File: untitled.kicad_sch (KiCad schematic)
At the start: 6 parts, among them J13 HDMI_A_1.4, J3 Bus_M.2_Socket_M, J5 USB3_A, J6 USB3_A, M1 M.2 Screw

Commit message: At home update
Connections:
- net GND: now also J5.10 (SHIELD), J5.A4 (GND), J5.A7 (DRAIN), J5.B4 (GND), J5.B7 (DRAIN), J6.10 (SHIELD), J6.A4 (GND), J6.A7 (DRAIN), J6.B4 (GND), J6.B7 (DRAIN), Module1.192 (GND)
- net at Module1.110 (PCIe_CLK_P): now also J3.55 (REFCLKp)
- net at Module1.112 (PCIe_CLK_N): now also J3.53 (REFCLKn)
- net +3.3v renamed +3.3V
- net +5v renamed +5V
- no-connect marks 105 -> 101

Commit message: Work Changes and documentation
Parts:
- removed J6: USB3_A, StackedUSBPretty:MOLEX_484060003, symbol Pi5Compute:USB3_A
- J5: footprint StackedUSBPretty:MOLEX_484060003 -> CM5IO:MTCONN_UBAF30-D2011
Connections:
- net Sim7600_DN renamed USB_DN
- net Sim7600_DP renamed USB_DP
- no-connect marks 101 -> 97

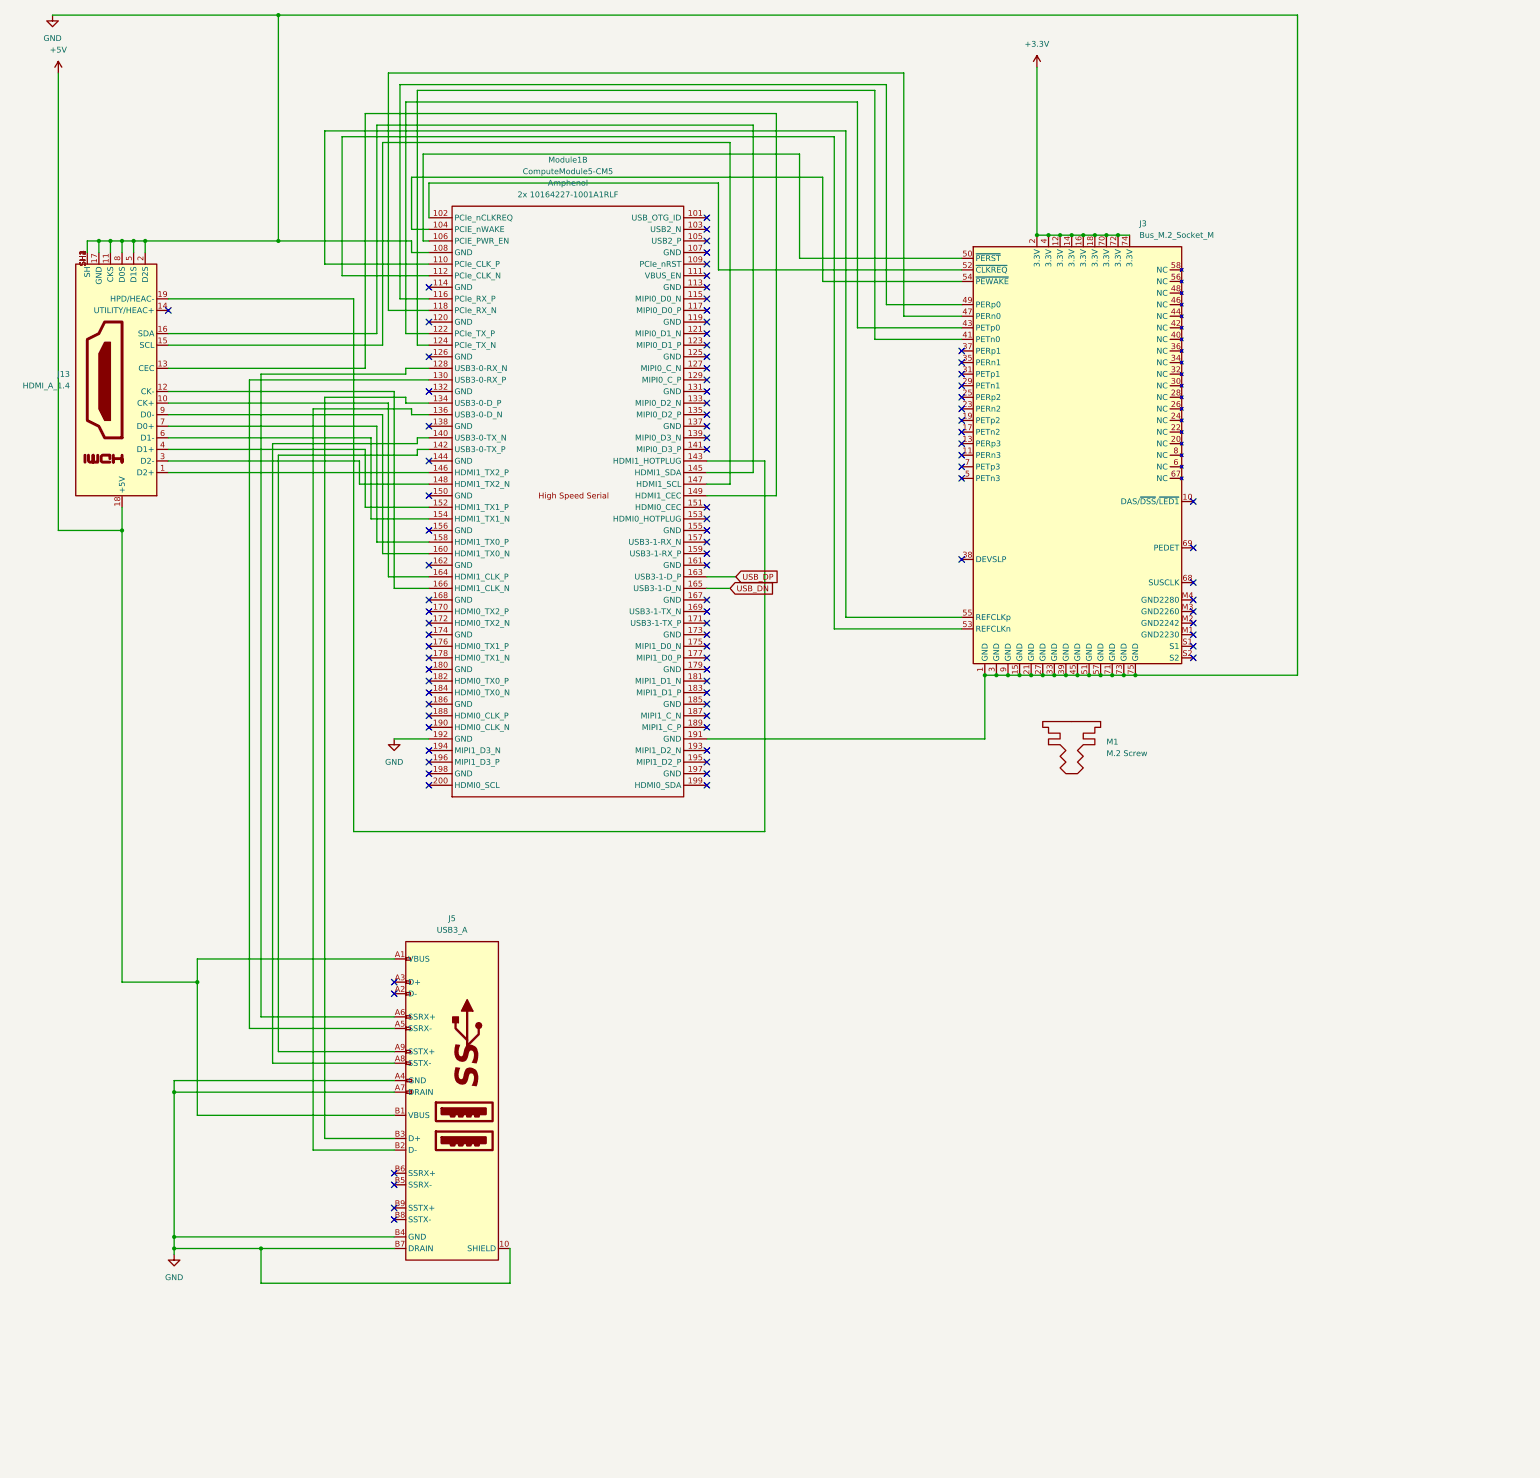
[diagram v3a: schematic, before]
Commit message: Updated to CM5 Doc
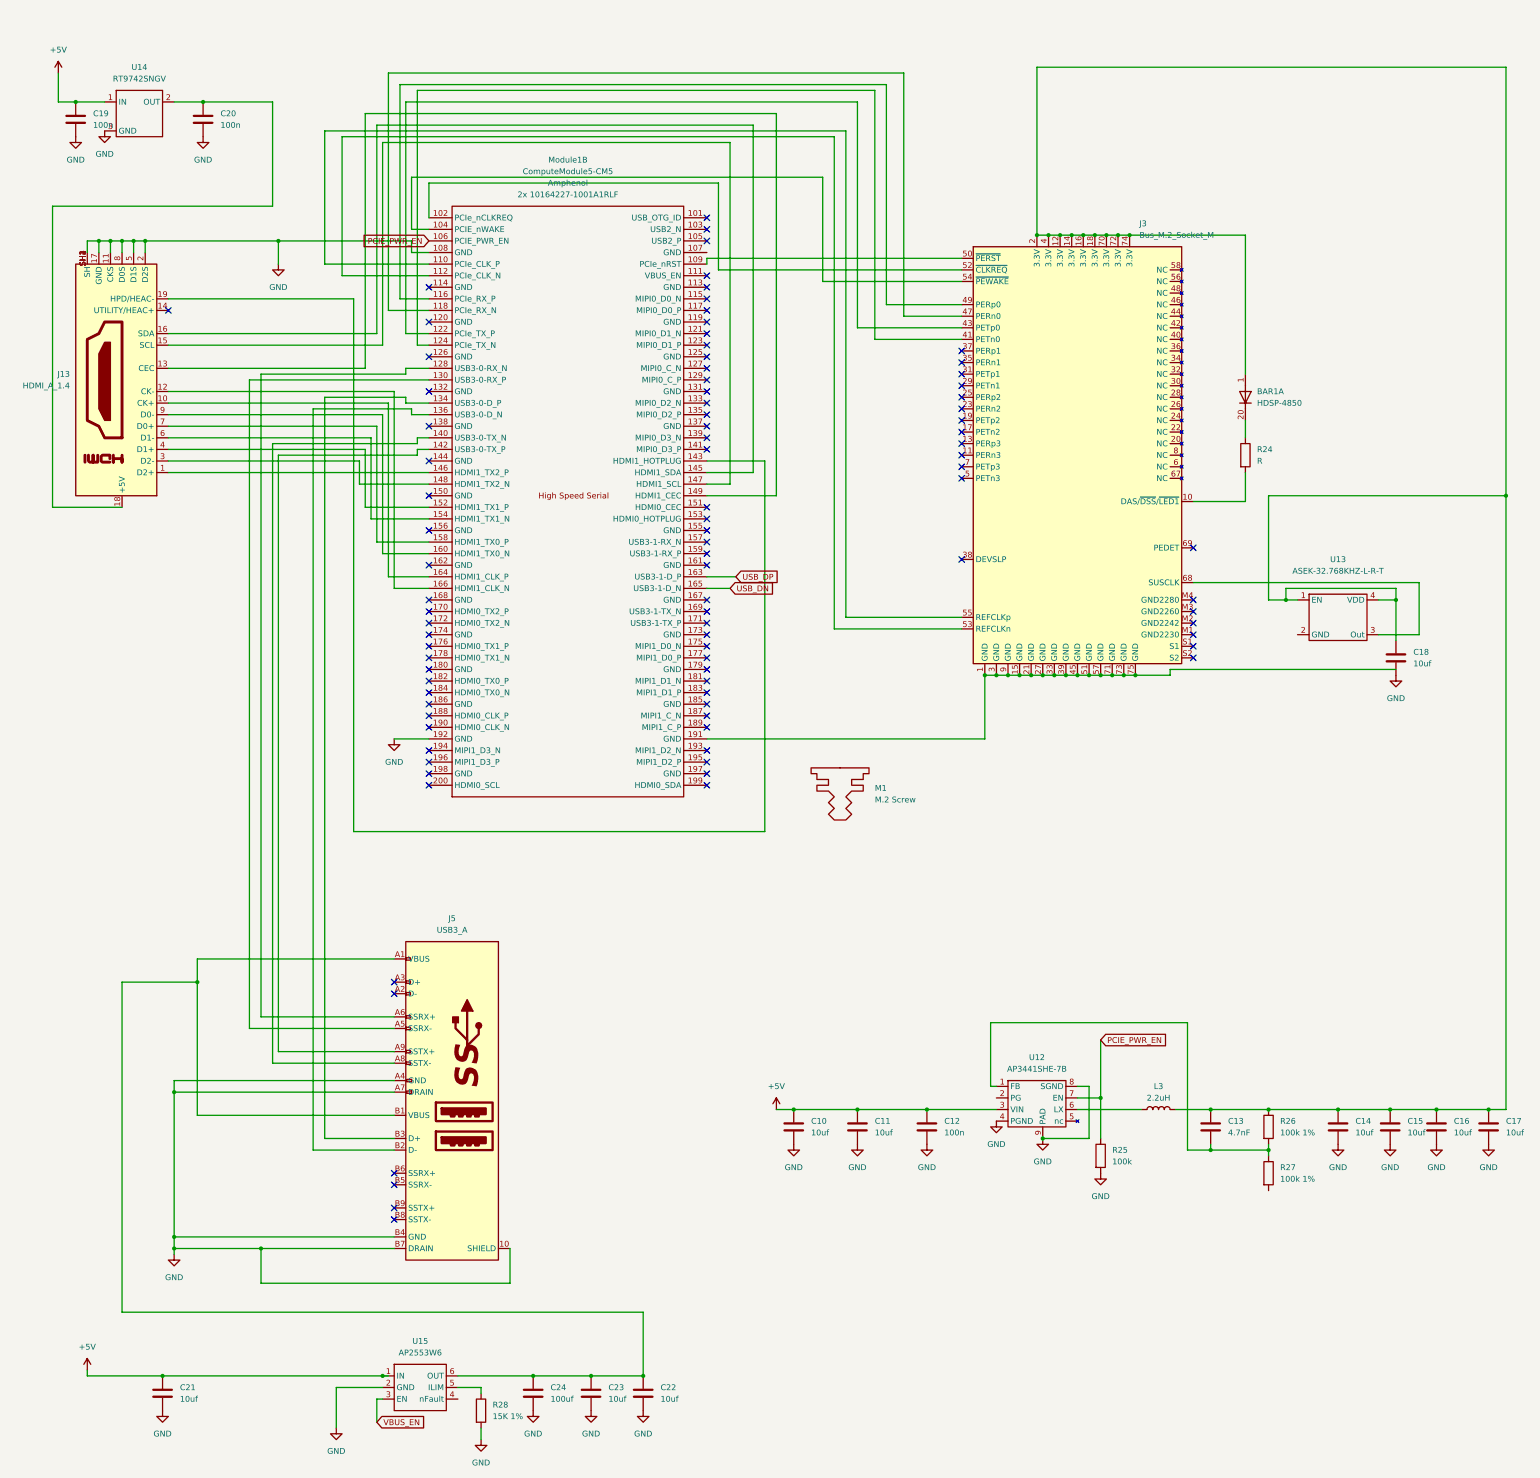
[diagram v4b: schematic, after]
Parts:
- added BAR1: HDSP-4850, Display:HDSP-4850, symbol LED:HDSP-4850
- added C10, C11, C14, C15, C16, C17, C18, C21, C22, C23: 10uf, symbol Device:C
- added C12, C19, C20: 100n, symbol Device:C
- added C13: 4.7nF, symbol Device:C
- added C24: 100uf, symbol Device:C
- added L3: 2.2uH, symbol Device:L
- added R24: R, symbol Device:R
- added R25: 100k, symbol Device:R
- added R26, R27: 100k 1%, symbol Device:R
- added R28: 15K 1%, symbol Device:R
- added U12: AP3441SHE-7B, Package_DFN_QFN:DFN-8-1EP_2x2mm_P0.5mm_EP1.05x1.75mm, symbol Pi5Compute:AP3441SHE-7B
- added U13: ASEK-32.768KHZ-L-R-T, Crystal:Crystal_SMD_3225-4Pin_3.2x2.5mm, symbol Pi5Compute:ASEK-32.768KHZ-L-R-T
- added U14: RT9742SNGV, Package_TO_SOT_SMD:TSOT-23_HandSoldering, symbol Pi5Compute:RT9742SNGV
- added U15: AP2553W6, Package_TO_SOT_SMD:SOT-23-6, symbol Pi5Compute:AP2553W6
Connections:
- net +5V: now also C10.1, C11.1, C12.1, C19.1, C21.1, U12.3 (VIN), U14.1 (IN), U15.1 (IN); no longer J13.18 (+5V), J5.A1 (VBUS), J5.B1 (VBUS)
- net GND: now also C10.2, C11.2, C12.2, C14.2, C15.2, C16.2, C17.2, C18.2, C19.2, C20.2, C21.2, C22.2, C23.2, C24.2, R25.2, R28.2, U12.4 (PGND), U12.8 (SGND), U12.9 (PAD), U14.3 (GND), U15.2 (GND); no longer J3.1 (GND), J3.15 (GND), J3.21 (GND), J3.27 (GND), J3.3 (GND), J3.33 (GND), J3.39 (GND), J3.45 (GND), J3.51 (GND), J3.57 (GND), J3.71 (GND), J3.73 (GND), J3.75 (GND), J3.9 (GND), Module1.191 (GND)
- net at J3.50 (~{PERST}): now also Module1.109 (PCIe_nRST); no longer Module1.106 (PCIE_PWR_EN)
- net at J3.10 (DAS/~{DSS}/~{LED1}): now also R24.2
- net at J3.68 (SUSCLK): now also U13.3 (Out)
- net +3.3V: no longer names the net of J3.12 (3.3V), J3.14 (3.3V), J3.16 (3.3V), J3.18 (3.3V), J3.2 (3.3V), J3.4 (3.3V), J3.70 (3.3V), J3.72 (3.3V), J3.74 (3.3V)
- net +3.3V: now also BAR1.1 (A), C13.1, C14.1, C15.1, C16.1, C17.1, C18.1, L3.2, R26.1, U13.1 (EN), U13.4 (VDD)
- new net: C22.1, C23.1, C24.1, J5.A1 (VBUS), J5.B1 (VBUS), U15.6 (OUT)
- new net: BAR1.20 (K), R24.1
- new net: R28.1, U15.5 (ILIM)
- new net: C20.1, J13.18 (+5V), U14.2 (OUT)
- new net: J3.1 (GND), J3.15 (GND), J3.21 (GND), J3.27 (GND), J3.3 (GND), J3.33 (GND), J3.39 (GND), J3.45 (GND), J3.51 (GND), J3.57 (GND), J3.71 (GND), J3.73 (GND), J3.75 (GND), J3.9 (GND), Module1.191 (GND)
- new net: C13.2, R26.2, R27.1, U12.1 (FB)
- new net: L3.1, U12.6 (LX)
- new net PCIE_PWR_EN: Module1.106 (PCIE_PWR_EN), R25.1, U12.7 (EN)
- new net VBUS_EN: U15.3 (EN)
- no-connect marks 97 -> 93
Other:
- moved on the sheet: M1

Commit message: fixed stuff at home
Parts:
- removed BAR1: HDSP-4850, Display:HDSP-4850, symbol LED:HDSP-4850
- added D1: LED, LED_SMD:LED_0805_2012Metric, symbol Device:LED
- C10, C11, C12, C13, C14, C15, C16, C17, C18, C19, C20, C21, C22, C23, C24: footprint (none) -> Capacitor_SMD:C_0805_2012Metric
- L3: footprint (none) -> Inductor_SMD:L_0805_2012Metric
- R24, R25, R26, R27, R28: footprint (none) -> Resistor_SMD:R_0805_2012Metric
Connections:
- net GND: now also R27.2
- net at C13.1, C14.1, C15.1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: now also D1.2 (A)
- net at R24.1: now also D1.1 (K)
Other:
- moved on the sheet: M1

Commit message: PCIE Changes
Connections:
- net GND: now also J3.1 (GND), J3.15 (GND), J3.21 (GND), J3.27 (GND), J3.3 (GND), J3.33 (GND), J3.39 (GND), J3.45 (GND), J3.51 (GND), J3.57 (GND), J3.71 (GND), J3.73 (GND), J3.75 (GND), J3.9 (GND), Module1.107 (GND), Module1.113 (GND), Module1.114 (GND), Module1.119 (GND), Module1.120 (GND), Module1.125 (GND), Module1.126 (GND), Module1.131 (GND), Module1.132 (GND), Module1.137 (GND), Module1.138 (GND), Module1.144 (GND), Module1.150 (GND), Module1.155 (GND), Module1.156 (GND), Module1.161 (GND), Module1.162 (GND), Module1.167 (GND), Module1.168 (GND), Module1.173 (GND), Module1.174 (GND), Module1.179 (GND), Module1.180 (GND), Module1.185 (GND), Module1.186 (GND), Module1.191 (GND), Module1.197 (GND), Module1.198 (GND), U13.2 (GND)
- net VBUS_EN: now also Module1.111 (VBUS_EN)
- net PER0_P: now reaches J3.49 (PER0_P)
- net PER0_P: now also Module1.124 (PCIe_TX_N); no longer Module1.116 (PCIe_RX_P)
- net PER0_N: now reaches J3.47 (PER0_N)
- net PER0_N: now also Module1.122 (PCIe_TX_P); no longer Module1.118 (PCIe_RX_N)
- net PET0_P: now reaches J3.43 (PET0_P)
- net PET0_P: now also Module1.118 (PCIe_RX_N); no longer Module1.122 (PCIe_TX_P)
- net PET0_N: now reaches J3.41 (PET0_N)
- net PET0_N: now also Module1.116 (PCIe_RX_P); no longer Module1.124 (PCIe_TX_N)
- no-connect marks 93 -> 68

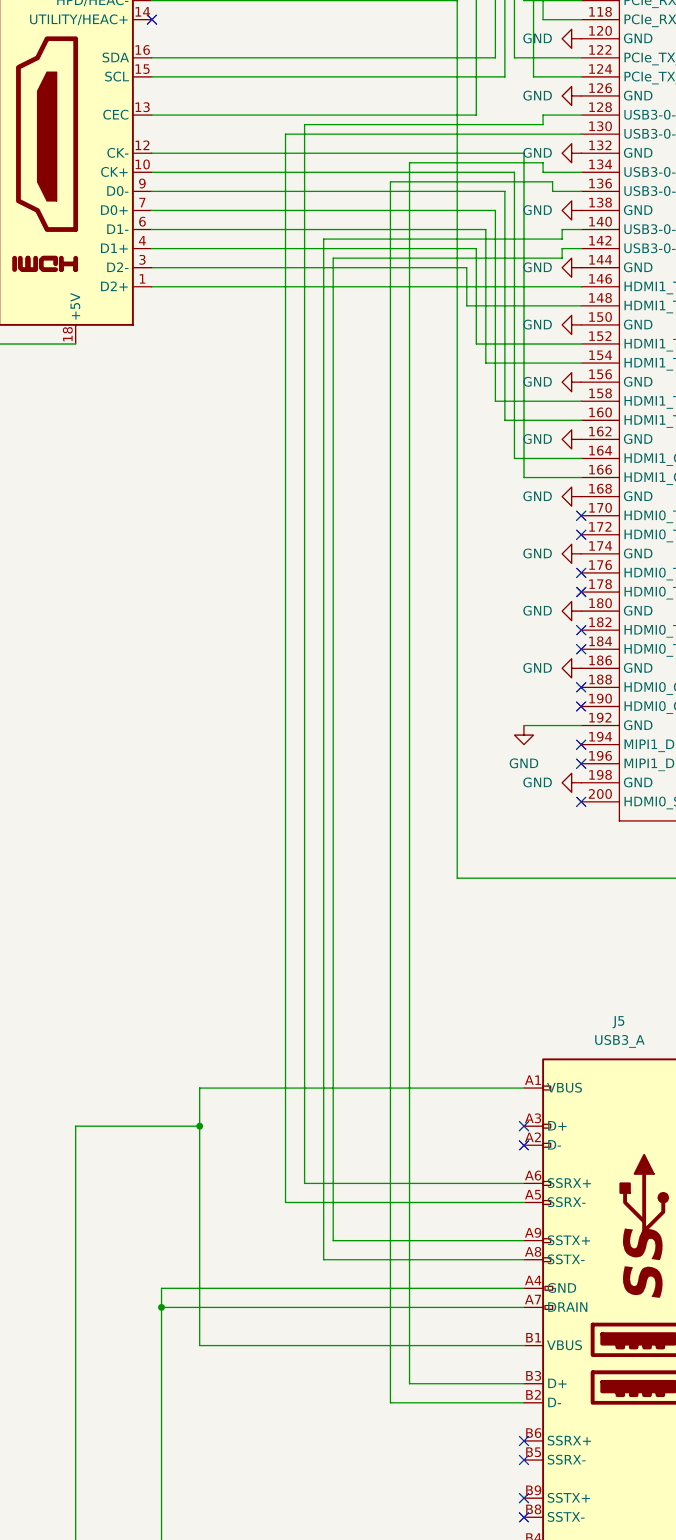
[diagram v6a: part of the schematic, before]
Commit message: Fixes from datasheets
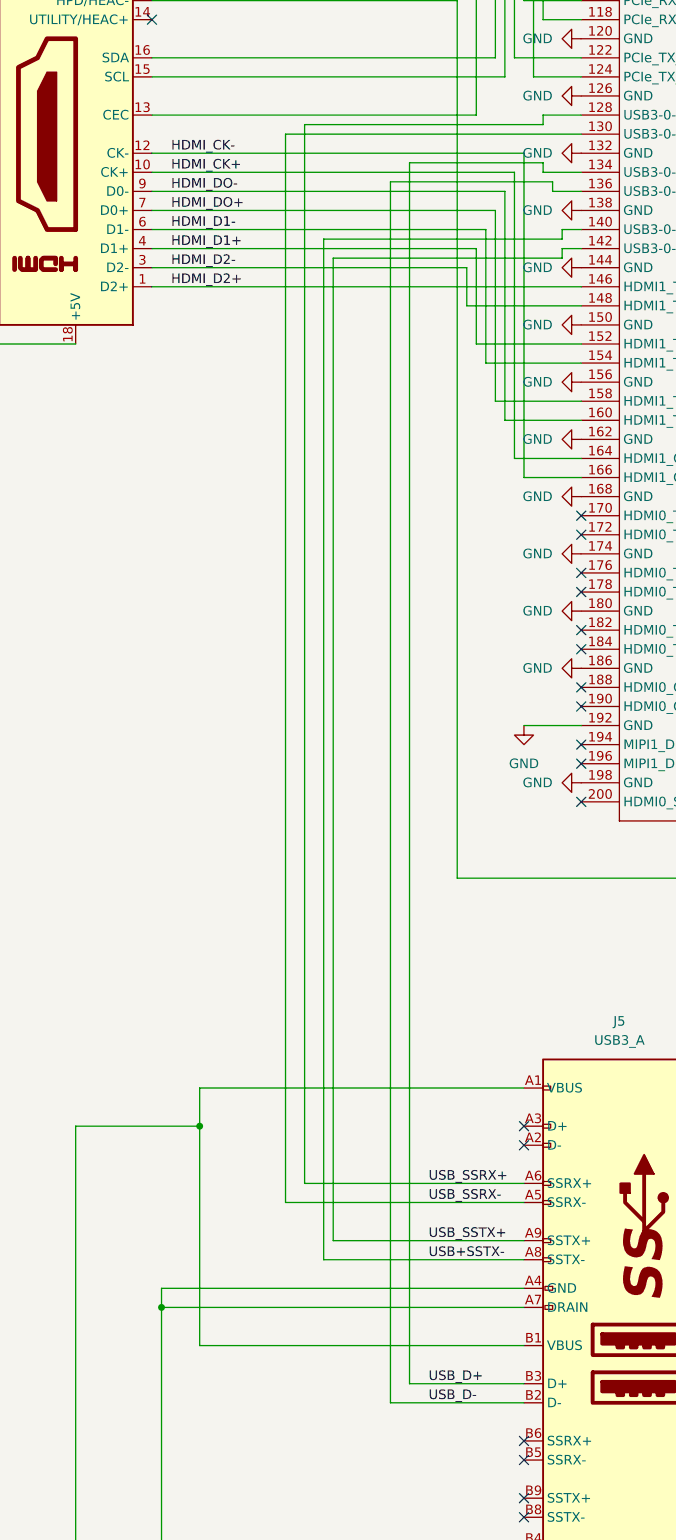
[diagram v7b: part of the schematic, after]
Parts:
- J13: footprint Connector_Video:HDMI_A_Amphenol_10029449-x01xLF_Horizontal -> CM5IO:EDAC 690-019-298-412
- U12: footprint Package_DFN_QFN:DFN-8-1EP_2x2mm_P0.5mm_EP1.05x1.75mm -> Package_DFN_QFN:DFN-8-1EP_3x3mm_P0.65mm_EP1.7x2.05mm
- U13: footprint Crystal:Crystal_SMD_3225-4Pin_3.2x2.5mm -> Crystal:Crystal_SMD_3225-4Pin_3.2x2.5mm_HandSoldering
- U15: footprint Package_TO_SOT_SMD:SOT-23-6 -> Package_TO_SOT_SMD:SOT-23-6_Handsoldering
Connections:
- net USB_SSRX-: now reaches J5.A5 (SSRX-), Module1.130 (USB3-0-RX_P)
- net USB_SSRX+: now reaches J5.A6 (SSRX+), Module1.128 (USB3-0-RX_N)
- net USB+SSTX-: now reaches J5.A8 (SSTX-), Module1.140 (USB3-0-TX_N)
- net USB_SSTX+: now reaches J5.A9 (SSTX+), Module1.142 (USB3-0-TX_P)
- net USB_D-: now reaches J5.B2 (D-), Module1.136 (USB3-0-D_N)
- net USB_D+: now reaches J5.B3 (D+), Module1.134 (USB3-0-D_P)
- net HDMI_D2+: now reaches J13.1 (D2+), Module1.146 (HDMI1_TX2_P)
- net HDMI_CK+: now reaches J13.10 (CK+), Module1.164 (HDMI1_CLK_P)
- net HDMI_CK-: now reaches J13.12 (CK-), Module1.166 (HDMI1_CLK_N)
- net HDMI_D2-: now reaches J13.3 (D2-), Module1.148 (HDMI1_TX2_N)
- net HDMI_D1+: now reaches J13.4 (D1+), Module1.152 (HDMI1_TX1_P)
- net HDMI_D1-: now reaches J13.6 (D1-), Module1.154 (HDMI1_TX1_N)
- net HDMI_DO+: now reaches J13.7 (D0+), Module1.158 (HDMI1_TX0_P)
- net HDMI_DO-: now reaches J13.9 (D0-), Module1.160 (HDMI1_TX0_N)
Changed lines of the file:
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@@
 	(wire
 		(pts
+			(xy 43.18 102.87) (xy 91.44 102.87)
+		)
+		(stroke
+			(width 0)
+			(type default)
+		)
+	)
+	(wire
+		(pts
 			(xy 93.98 33.02) (xy 93.98 90.17)
 		)
@@
 	(wire
 		(pts
-			(xy 91.44 102.87) (xy 43.18 102.87)
-		)
-		(stroke
-			(width 0)
-			(type default)
-		)
-	)
-	(wire
-		(pts
 			(xy 81.28 44.45) (xy 81.28 74.93)
 		)
@@
 		)
 	)
+	(label "USB_D+"
+		(at 80.01 264.16 0)
+		(effects
+			(font
+				(size 1.27 1.27)
+			)
+			(justify left bottom)
+		)
+	)
+	(label "USB+SSTX-"
+		(at 80.01 247.65 0)
+		(effects
+			(font
+				(size 1.27 1.27)
+			)
+			(justify left bottom)
+		)
+	)
+	(label "USB_SSRX+"
+		(at 80.01 237.49 0)
+		(effects
+			(font
+				(size 1.27 1.27)
+			)
+			(justify left bottom)
+		)
+	)
+	(label "USB_SSTX+"
+		(at 80.01 245.11 0)
+		(effects
+			(font
+				(size 1.27 1.27)
+			)
+			(justify left bottom)
+		)
+	)
 	(label "PER0_N"
 		(at 208.28 83.82 0)
@@
 		)
 	)
+	(label "HDMI_CK+"
+		(at 45.72 102.87 0)
+		(effects
+			(font
+				(size 1.27 1.27)
+			)
+			(justify left bottom)
+		)
+	)
+	(label "HDMI_D2-"
+		(at 45.72 115.57 0)
+		(effects
+			(font
+				(size 1.27 1.27)
+			)
+			(justify left bottom)
+		)
+	)
+	(label "HDMI_CK-"
+		(at 45.72 100.33 0)
+		(effects
+			(font
+				(size 1.27 1.27)
+			)
+			(justify left bottom)
+		)
+	)
 	(label "PET0_P"
 		(at 209.55 86.36 0)
@@
 		)
 	)
+	(label "HDMI_D1-"
+		(at 45.72 110.49 0)
+		(effects
+			(font
+				(size 1.27 1.27)
+			)
+			(justify left bottom)
+		)
+	)
+	(label "HDMI_DO-"
+		(at 45.72 105.41 0)
+		(effects
+			(font
+				(size 1.27 1.27)
+			)
+			(justify left bottom)
+		)
+	)
+	(label "USB_D-"
+		(at 80.01 266.7 0)
+		(effects
+			(font
+				(size 1.27 1.27)
+			)
+			(justify left bottom)
+		)
+	)
+	(label "USB_SSRX-"
+		(at 80.01 240.03 0)
+		(effects
+			(font
+				(size 1.27 1.27)
+			)
+			(justify left bottom)
+		)
+	)
+	(label "HDMI_D2+"
+		(at 45.72 118.11 0)
+		(effects
+			(font
+				(size 1.27 1.27)
+			)
+			(justify left bottom)
+		)
+	)
 	(label "PER0_P"
 		(at 208.28 81.28 0)
@@
 		)
 	)
+	(label "HDMI_D1+"
+		(at 45.72 113.03 0)
+		(effects
+			(font
+				(size 1.27 1.27)
+			)
+			(justify left bottom)
+		)
+	)
+	(label "HDMI_DO+"
+		(at 45.72 107.95 0)
+		(effects
+			(font
+				(size 1.27 1.27)
+			)
+			(justify left bottom)
+		)
+	)
 	(global_label "PCIE_PWR_EN"
 		(shape input)
@@
 			)
 		)
-		(property "Footprint" "Connector_Video:HDMI_A_Amphenol_10029449-x01xLF_Horizontal"
+		(property "Footprint" "CM5IO:EDAC 690-019-298-412"
 			(at 32.385 97.79 0)
 			(effects
@@
 			)
 		)
-		(property "Footprint" "Package_TO_SOT_SMD:SOT-23-6"
+		(property "Footprint" "Package_TO_SOT_SMD:SOT-23-6_Handsoldering"
 			(at 102.87 325.12 0)
 			(effects
@@
 			)
 		)
-		(property "Footprint" "Crystal:Crystal_SMD_3225-4Pin_3.2x2.5mm"
+		(property "Footprint" "Crystal:Crystal_SMD_3225-4Pin_3.2x2.5mm_HandSoldering"
 			(at 300.99 158.75 0)
 			(effects
@@
 			)
 		)
-		(property "Footprint" "Package_DFN_QFN:DFN-8-1EP_2x2mm_P0.5mm_EP1.05x1.75mm"
+		(property "Footprint" "Package_DFN_QFN:DFN-8-1EP_3x3mm_P0.65mm_EP1.7x2.05mm"
 			(at 234.95 265.43 0)
 			(effects
